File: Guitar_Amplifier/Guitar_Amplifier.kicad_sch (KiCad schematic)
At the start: 12 parts, among them J1 Conn_01x04, J2 Conn_01x02, U1 LM386

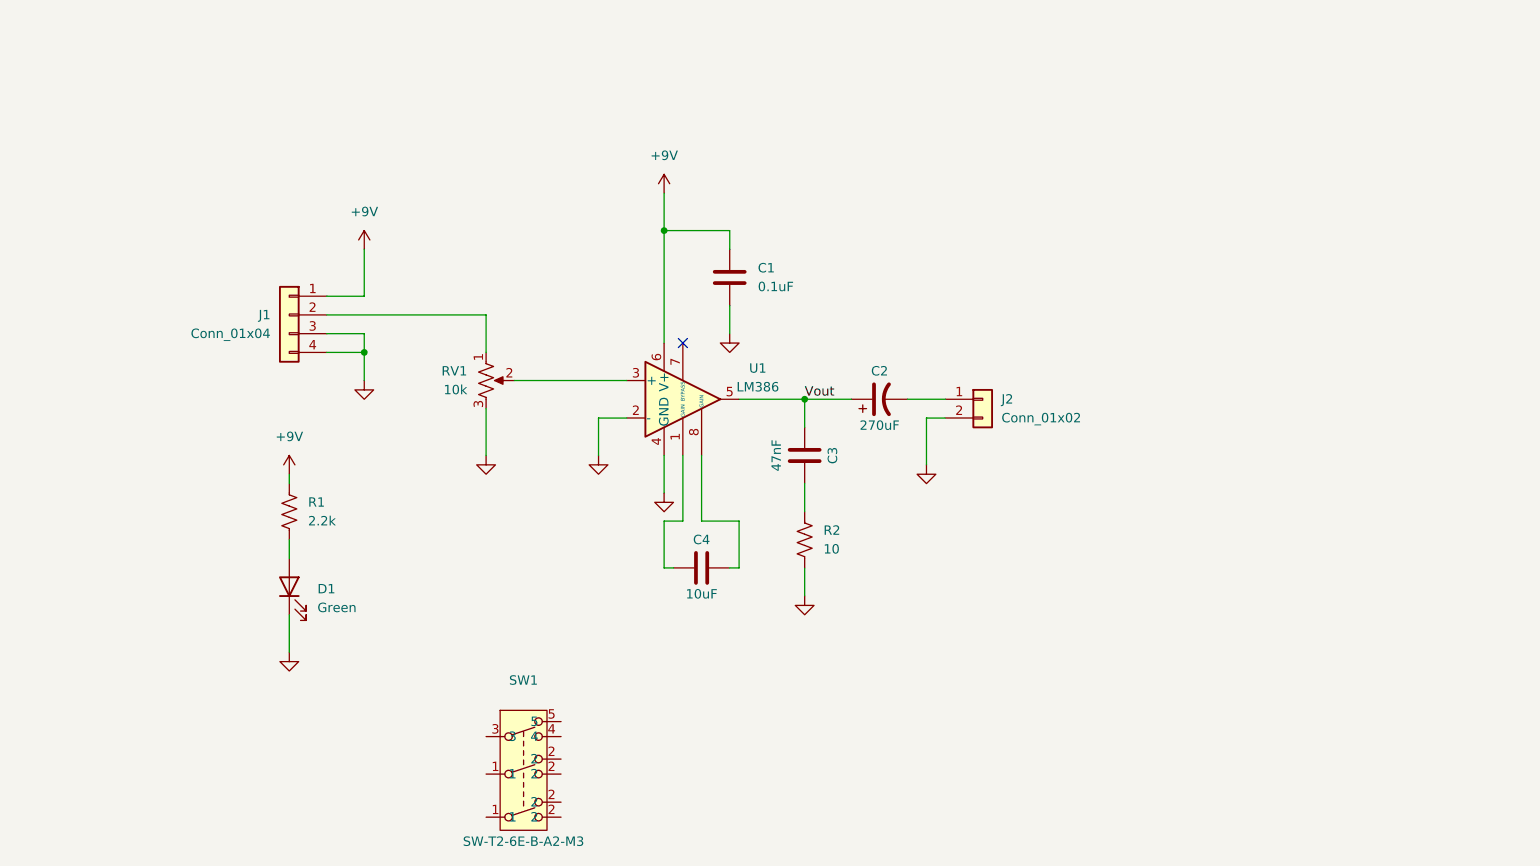
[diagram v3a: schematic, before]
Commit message: Added in switch symbol and footprint
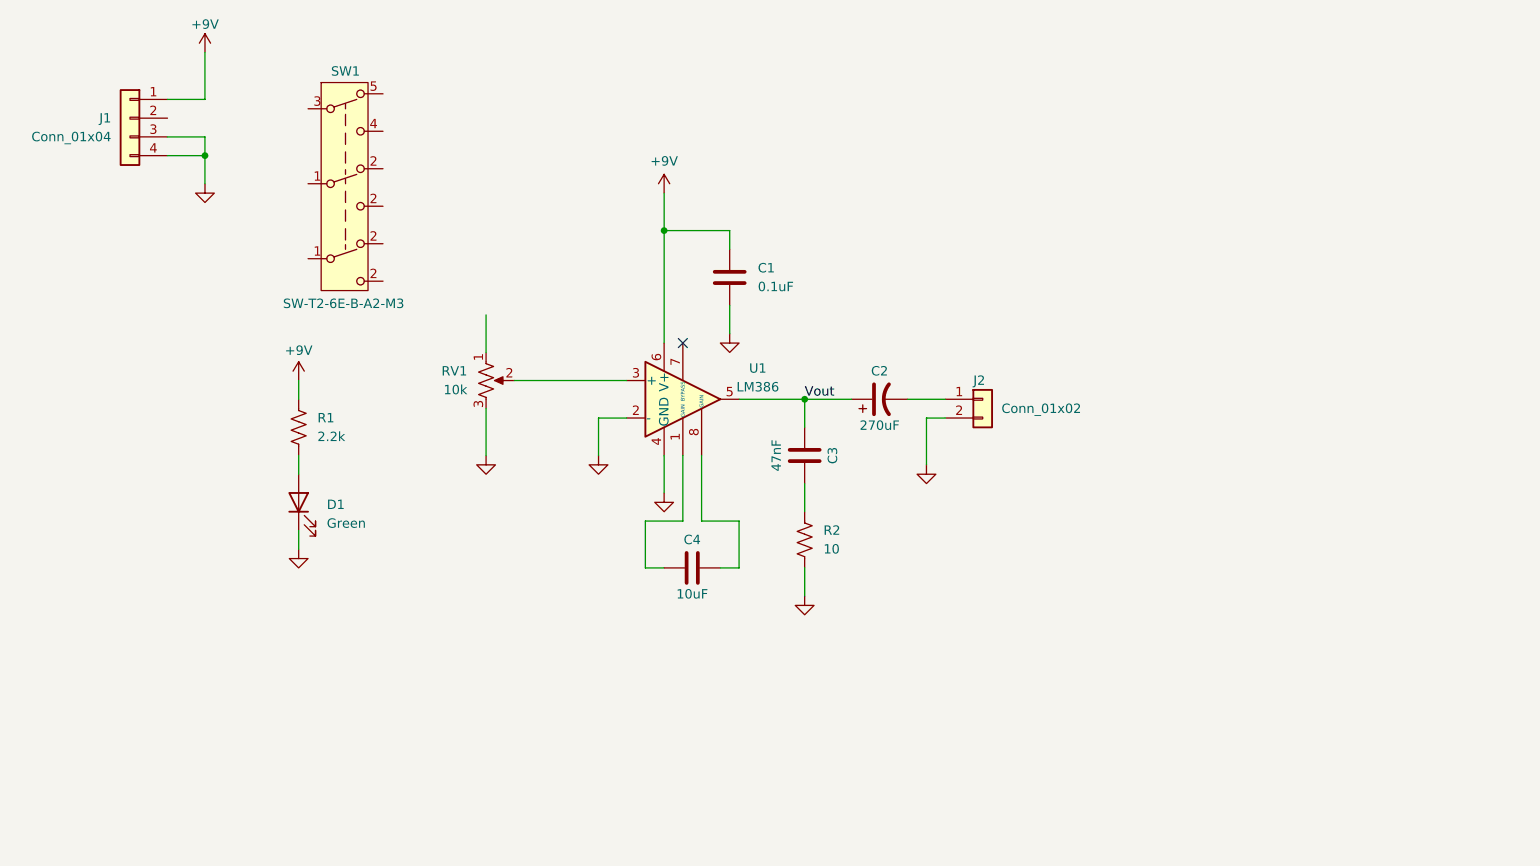
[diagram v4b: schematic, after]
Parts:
- SW1: footprint (none) -> RG_Switches_footprints:3PDT Switch
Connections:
- net at RV1.1: no longer J1.2 (Pin_2)
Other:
- moved on the sheet: C4, D1, J1, R1

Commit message: Added additional symbols
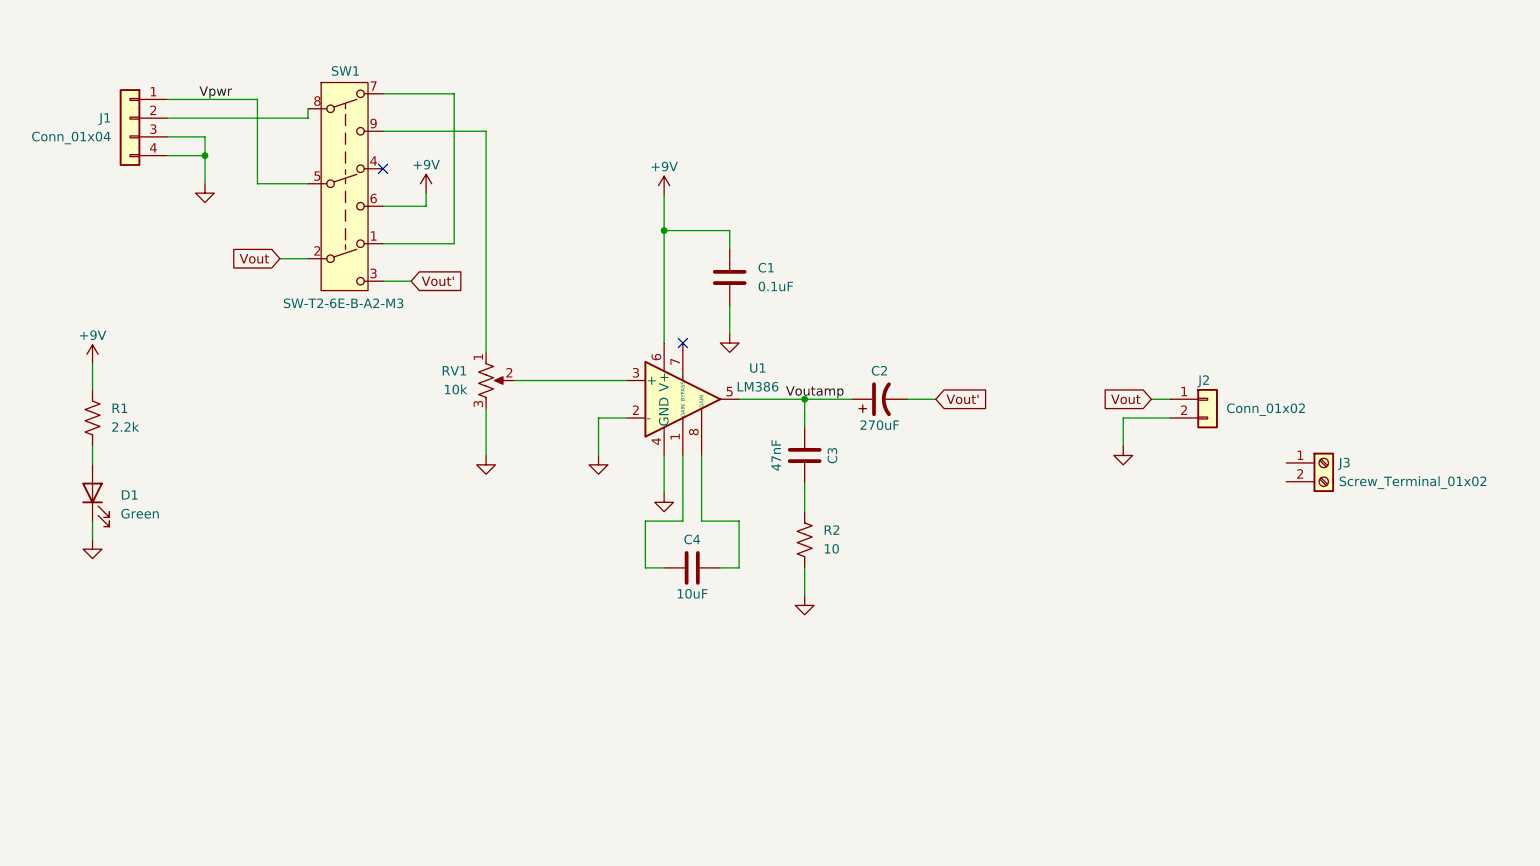
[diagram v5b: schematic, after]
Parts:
- added J3: Screw_Terminal_01x02, symbol Connector:Screw_Terminal_01x02
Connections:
- net +9V: now also SW1.6; no longer J1.1 (Pin_1)
- net Vout: now also J2.1 (Pin_1), SW1.2; no longer C2.1, C3.2, U1.5
- net at RV1.1: now also SW1.9
- net at J1.2 (Pin_2): now also SW1.8
- net Vout': now reaches C2.2
- net Vout': now also SW1.3; no longer J2.1 (Pin_1)
- net at SW1.1: now also SW1.7
- net Vpwr: now reaches SW1.5
- net Vpwr: now also J1.1 (Pin_1)
- new net Voutamp: C2.1, C3.2, U1.5
- no-connect marks 1 -> 2
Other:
- moved on the sheet: D1, J2, R1
